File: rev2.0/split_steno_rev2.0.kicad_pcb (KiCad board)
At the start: 2 copper layers, 71 parts, among them J1 Audio-Jack-4, J2 USB_OTG, P1 TC2030-IDC, SW1 SW_Push, SW10 SW_Push, SW11 SW_Push, SW12 SW_Push, SW13 SW_Push, SW14 SW_Push, SW15 SW_Push, SW16 SW_Push, SW17 SW_Push, SW18 SW_Push, SW19 SW_Push, SW2 SW_Push, SW20 SW_Push, SW21 SW_Push, SW22 Switch-6P-2S2T, SW3 SW_Push, SW4 SW_Push, SW5 SW_Push, SW6 SW_Push, SW7 SW_Push, SW8 SW_Push, SW9 SW_Push, U1 74LVC1G34, U2 MCP73831, U3 MCP1700, U4 MCP1700, U5 ATXMEGA128A4U-AU, U6 nRF24L01_module

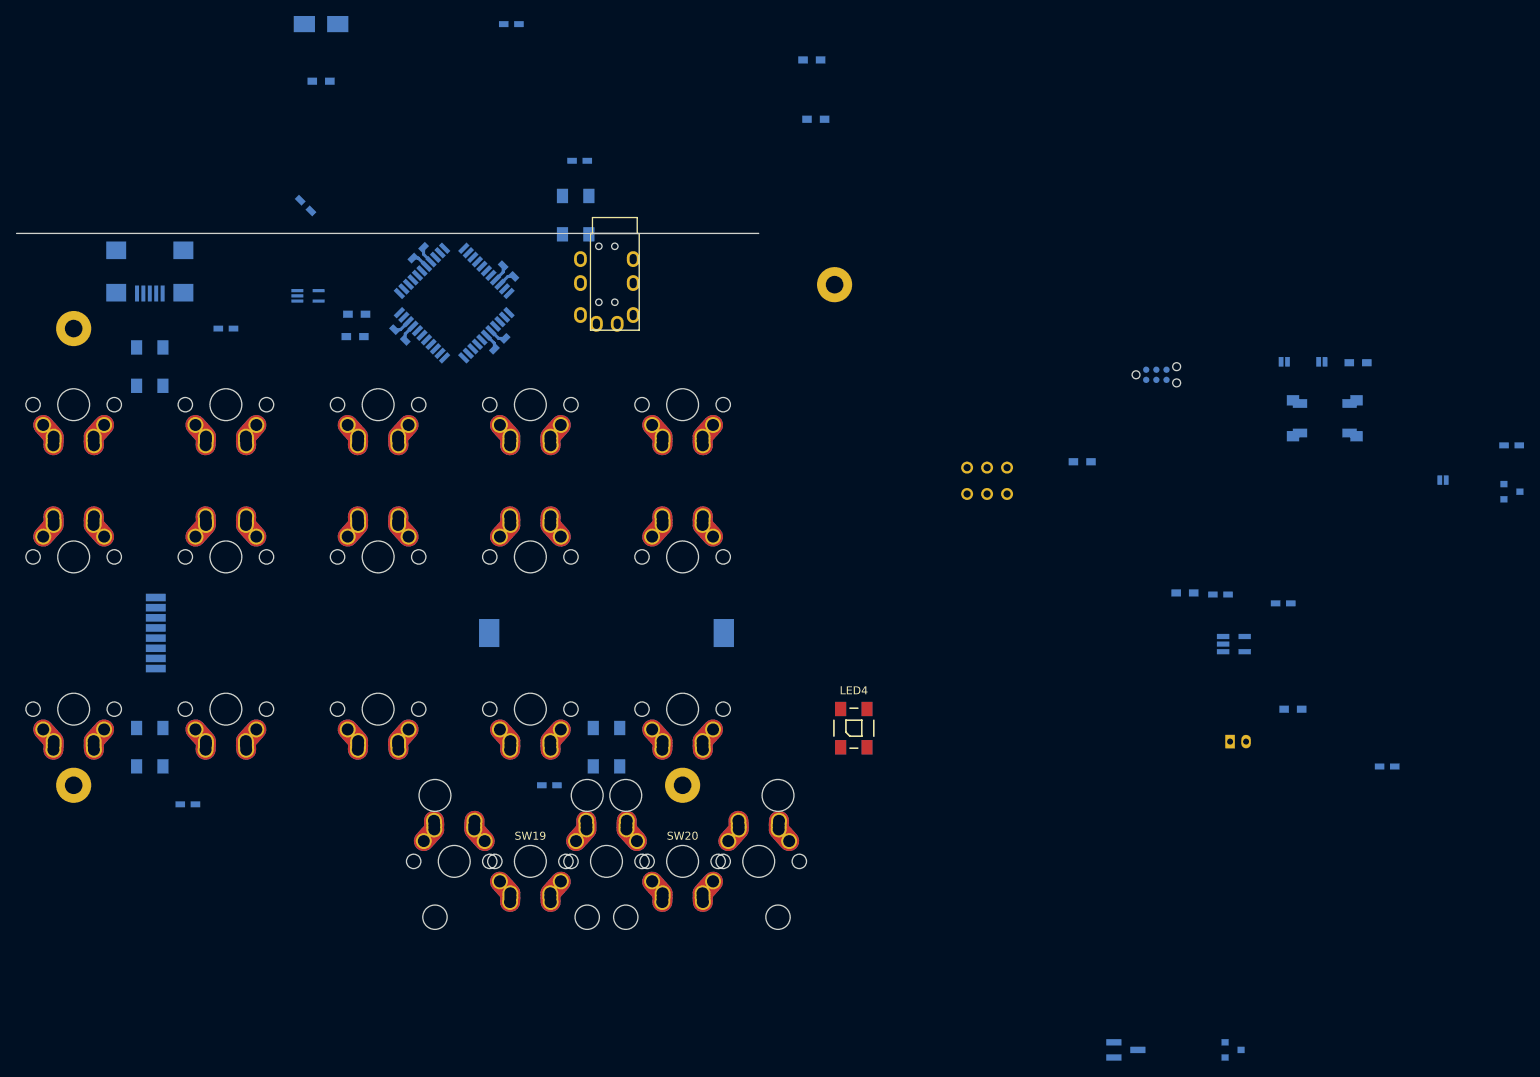
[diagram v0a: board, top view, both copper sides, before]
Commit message: reduced components, laid out pcb
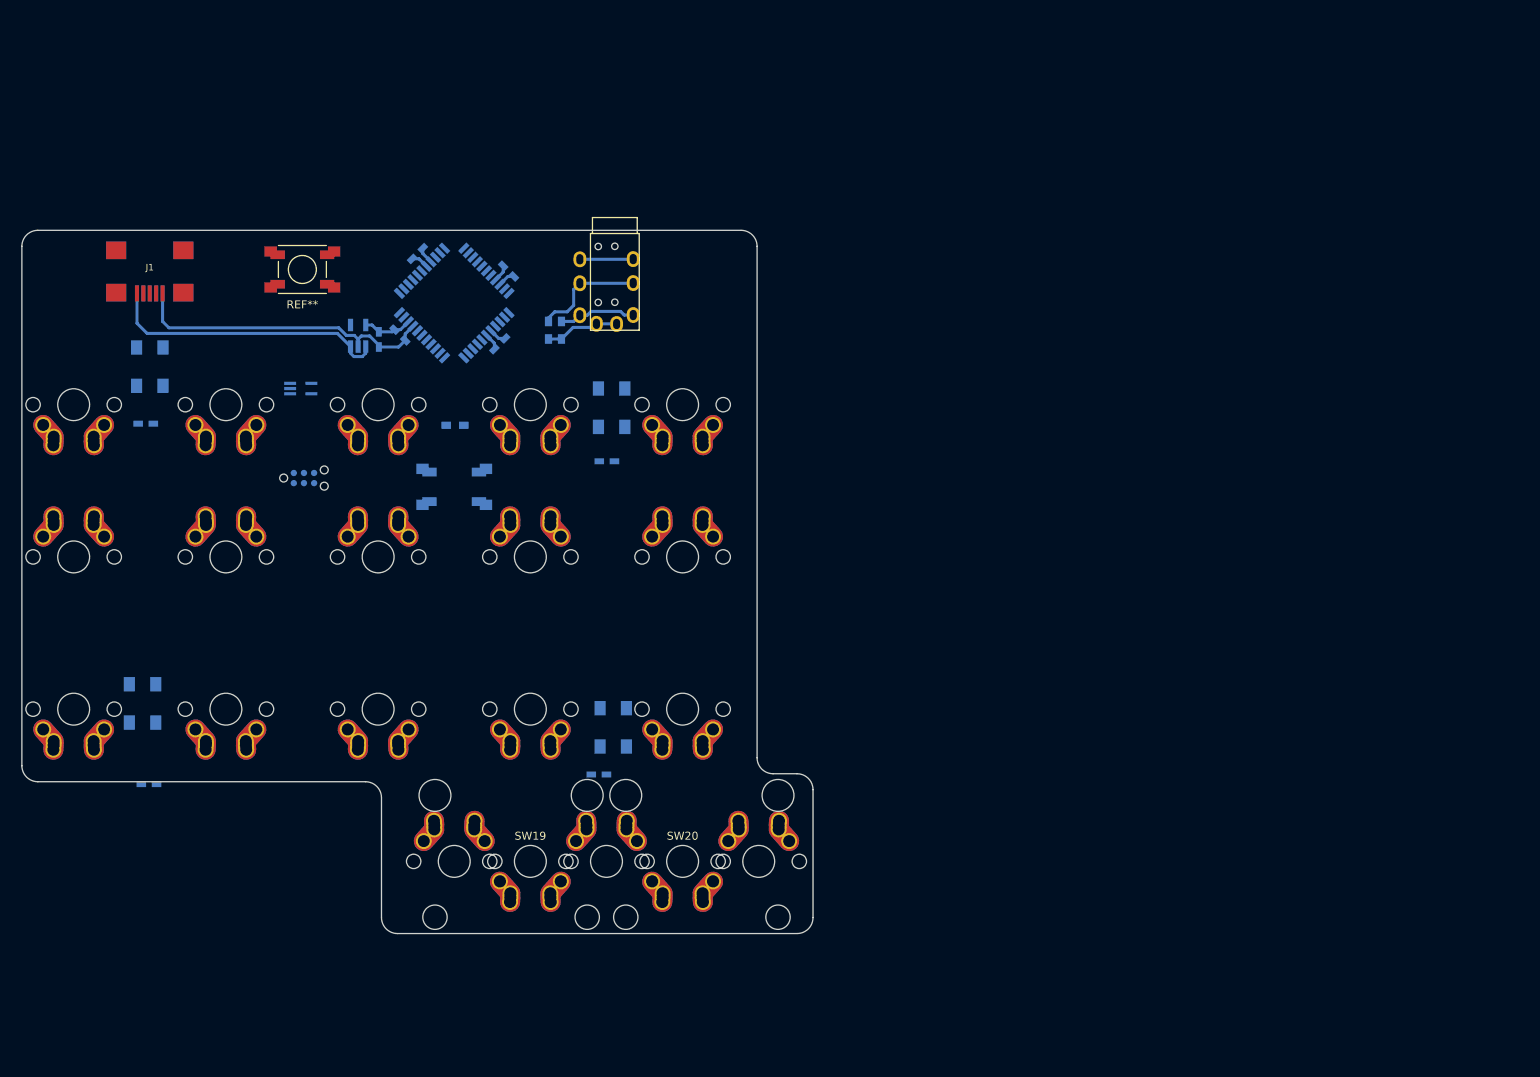
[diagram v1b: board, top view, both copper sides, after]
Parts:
- removed BT1: Battery, Battery_Holders:Keystone_1058_1x2032-CoinCell
- removed BT2: Battery_Cell, Connectors_JST:JST_PH_S2B-PH-K_02x2.00mm_Angled
- removed C10, C11, C12: 0.1uF, Capacitors_SMD:C_0603_HandSoldering
- removed C13: 10uF, Capacitors_SMD:C_0603_HandSoldering
- removed C14: 47uF, Capacitors_SMD:C_0603_HandSoldering
- removed D1: D_Schottky_x2_KCom_AAK, TO_SOT_Packages_SMD:SOT-23_Handsoldering
- removed F1: Fuse, Fuse_Holders_and_Fuses:Fuse_SMD1206_HandSoldering
- removed JP1, JP2, JP3: Jumper, keyboard_parts:SOLDER_JUMPER_2
- removed the LED4 at (138.1, 114.3)
- removed R3: 470k, Resistors_SMD:R_0603_HandSoldering
- removed R5, R8: 100k, Resistors_SMD:R_0603_HandSoldering
- removed R6: 10k, Resistors_SMD:R_0603_HandSoldering
- removed R7, R9: 4.7k, Resistors_SMD:R_0603_HandSoldering
- removed the REF** at (116.7, 121.4)
- removed the REF** at (40.5, 121.4)
- removed the REF** at (135.7, 58.8)
- removed the REF** at (40.5, 64.3)
- removed SW22: Switch-6P-2S2T, switch:SlideSwitch_C&K_JS202011CQN
- removed U4: MCP1700, TO_SOT_Packages_SMD:SOT-23
- removed U5: ATXMEGA128A4U-AU, Housings_QFP:TQFP-44_10x10mm_Pitch0.8mm
- removed U6: nRF24L01_module, nordic:NRF24L01-Module-SMD
- added G***: LOGO, airi_logo:airi_icon-7.6, B.Cu at (88.0, 61.0)
- added J1: USB_B, keyboard_parts:USB_miniB, F.Cu at (50.0, 57.1)
- added REF**: SwitchPush_C&K_RS-187R05A2-DS, switch:SwitchPush_C&K_MultiFoot_RS-187R05A2-DS_And_PTS645_SMT, F.Cu at (69.1, 56.9)
- C1, C6: value 4.7uF -> 0.1uF
- C5: value 0.1uF -> 10uF
- C7, C8: value 1uF -> 0.1uF
- R1: value 10k -> 4.7k
- R2: value 470k -> 4.7k
- R4: value 100k -> 10k
- U2: value MCP73831 -> MIC550X
- U3: value MCP1700 -> ATXMEGA128A4U-AU; footprint TO_SOT_Packages_SMD:SOT-23 -> Housings_QFP:TQFP-44_10x10mm_Pitch0.8mm
- moved C8 137.3 mm to (83.5, 54.9), turned to 225 degrees
- moved C1 136.2 mm to (49.5, 76.2)
- moved U3 135.0 mm to (88.1, 61.1), turned to 45 degrees
- moved C6 127.3 mm to (93.8, 66.2), turned to 45 degrees
- moved U2 116.2 mm to (76.1, 65.2), turned to 90 degrees
- moved C7 115.5 mm to (81.3, 65.1), turned to 315 degrees
- moved SW21 109.3 mm to (88.1, 84.1)
- moved P1 107.4 mm to (69.3, 83.0)
- moved R2 103.1 mm to (101.5, 64.5), turned to 90 degrees
- moved R1 101.4 mm to (99.9, 64.5), turned to 90 degrees
- moved LED2 81.7 mm to (49.1, 111.2)
- moved LED3 58.0 mm to (108.0, 114.2)
- moved LED4 42.5 mm to (107.8, 74.2)
- moved C4 37.8 mm to (107.2, 80.9)
- moved C5 19.2 mm to (78.7, 65.7), turned to 270 degrees
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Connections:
- C5 pad 1: +5V -> VCC
- C6 pad 1: /BAT_LI_ION -> VCC
- C7 pad 1: /BAT_IN -> VCC
- C8 pad 1: Net-(C8-Pad1) -> VCC
- J2 pad 1: Net-(F1-Pad1) -> +5V
- R1 pad 1: Net-(R1-Pad1) -> +3V3
- R1 pad 2: /BAT_PROG -> /SDA
- R2 pad 1: /BAT_LI_ION -> +3V3
- R2 pad 2: /BAT_LVL -> /SCL
- R4 pad 1: +5V -> VCC
- R4 pad 2: /VBUS_CHECK -> /RST
- REF** pad 1: (no net) -> +3V3
- REF** pad 2: (no net) -> /SCL
- REF** pad 3: (no net) -> /SDA
- REF** pad 4: (no net) -> GND
- U2 pad 1: /BAT_STAT -> +5V
- U2 pad 3: /BAT_LI_ION -> +5V
- U2 pad 4: +5V -> Net-(U2-Pad4)
- U2 pad 5: Net-(R1-Pad1) -> VCC
- U3 pad 1: GND -> /KEY16
- U3 pad 2: /BAT_IN -> /KEY17
- U3 pad 3: /BAT_LI_ION -> /KEY18
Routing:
- net GND: track 8.65 -> 52.3 mm
- net +5V: track 0.00 -> 35.6 mm
- net /SDA: track 0.00 -> 14.0 mm
- net /SCL: track 0.00 -> 9.68 mm
- net +3V3: track 0.00 -> 9.32 mm
- net VCC: track 8.66 -> 12.7 mm
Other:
- board outline added: 99 x 88 mm
